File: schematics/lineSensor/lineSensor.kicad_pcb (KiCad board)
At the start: 2 copper layers, 32 parts, among them P1 CONN_01X01, P10 CONN_01X01, P2 CONN_01X01, P3 CONN_01X01, P4 CONN_01X01, P5 CONN_01X01, P6 CONN_01X01, P7 CONN_01X01, P8 CONN_01X01, P9 CONN_01X01

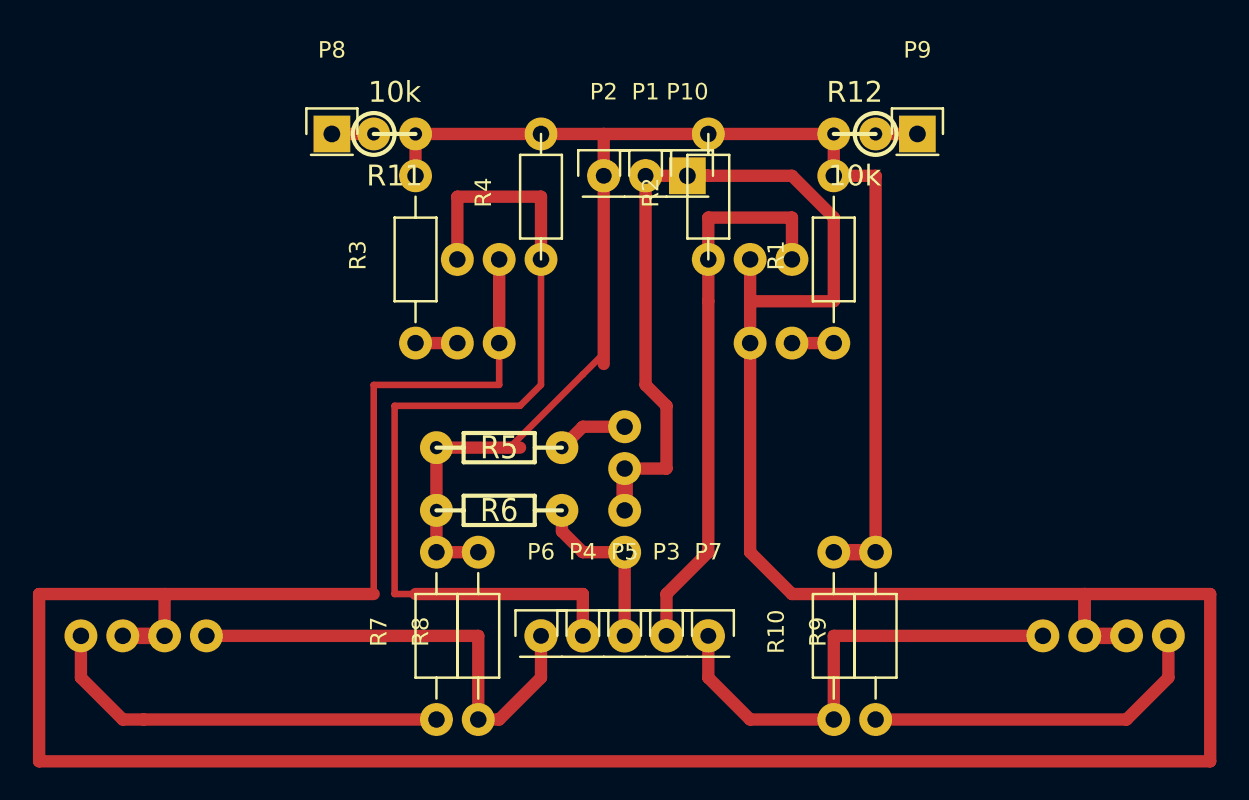
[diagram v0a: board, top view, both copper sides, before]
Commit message: Update lineSensor board for sonar power
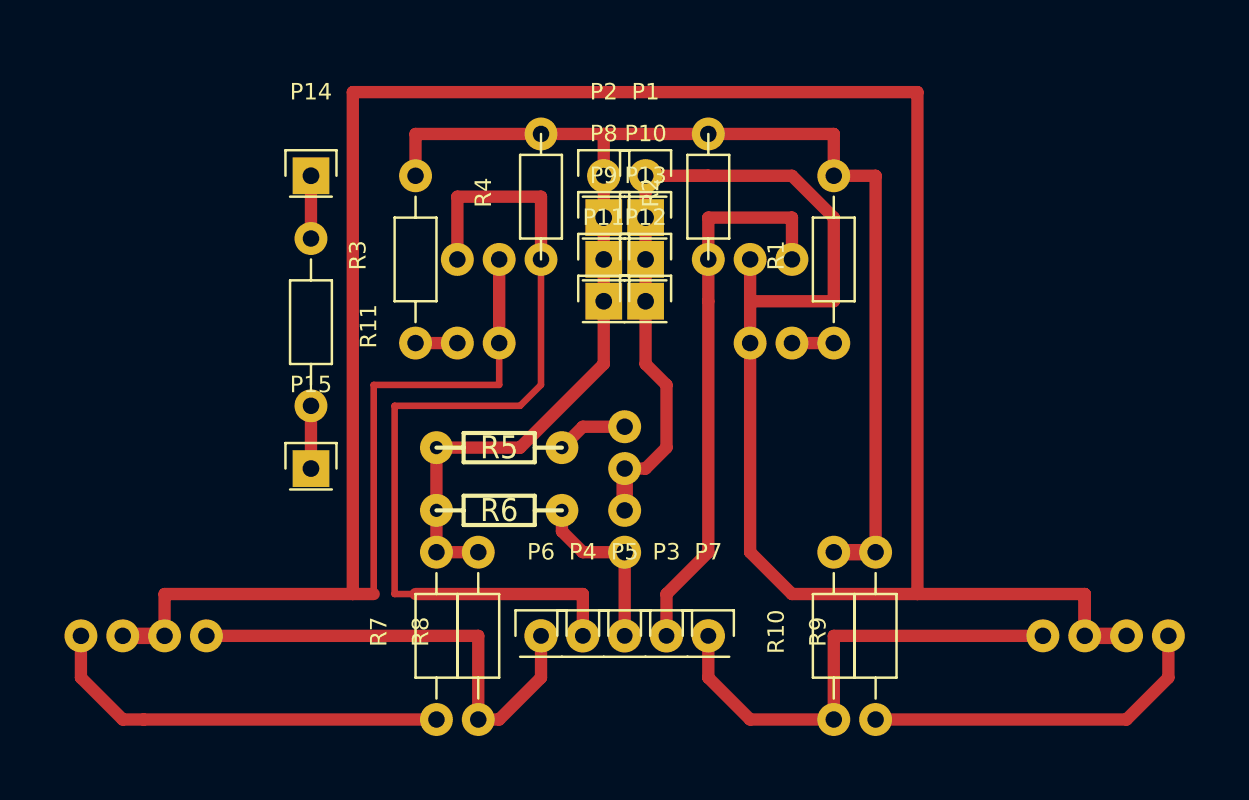
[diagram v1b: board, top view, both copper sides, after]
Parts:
- removed R12: 10k, w_pth_resistors:rc05_vert
- added P11: CONN_01X01, Pin_Headers:Pin_Header_Straight_1x01, F.Cu at (146.1, 109.2)
- added P12: CONN_01X01, Pin_Headers:Pin_Header_Straight_1x01, F.Cu at (148.6, 109.2)
- added P13: CONN_01X01, Pin_Headers:Pin_Header_Straight_1x01, F.Cu at (148.6, 106.7)
- added P14: CONN_01X01, Pin_Headers:Pin_Header_Straight_1x01, F.Cu at (128.3, 101.6)
- added P15: CONN_01X01, Pin_Headers:Pin_Header_Straight_1x01, F.Cu at (128.3, 119.4)
- R11: value 10k -> 8k2; footprint w_pth_resistors:rc05_vert -> Resistors_ThroughHole:Resistor_Horizontal_RM10mm
- moved P9 20.5 mm to (146.1, 106.7)
- moved P8 17.3 mm to (146.1, 104.1)
- moved R11 8.13 mm to (128.3, 105.4), turned to 270 degrees
- moved P10 3.59 mm to (148.6, 104.1)
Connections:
- P2 pad 1: Net-(P2-Pad1) -> Net-(P11-Pad1)
- P8 pad 1: Net-(P8-Pad1) -> Net-(P11-Pad1)
- P9 pad 1: Net-(P9-Pad1) -> Net-(P11-Pad1)
- R1 pad 2: Net-(P2-Pad1) -> Net-(P11-Pad1)
- R10 pad 2: Net-(P2-Pad1) -> Net-(P11-Pad1)
- R11 pad 1: Net-(P8-Pad1) -> Net-(P14-Pad1)
- R11 pad 2: Net-(P2-Pad1) -> Net-(P15-Pad1)
- R2 pad 2: Net-(P2-Pad1) -> Net-(P11-Pad1)
- R3 pad 2: Net-(P2-Pad1) -> Net-(P11-Pad1)
- R4 pad 2: Net-(P2-Pad1) -> Net-(P11-Pad1)
- R5 pad 2: Net-(P2-Pad1) -> Net-(P11-Pad1)
- R6 pad 2: Net-(P2-Pad1) -> Net-(P11-Pad1)
- R7 pad 2: Net-(P2-Pad1) -> Net-(P11-Pad1)
- R8 pad 2: Net-(P2-Pad1) -> Net-(P11-Pad1)
- R9 pad 2: Net-(P2-Pad1) -> Net-(P11-Pad1)
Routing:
- net Net-(P2-Pad1): track 109.7 -> 0.00 mm
- net Net-(P11-Pad1): track 0.00 -> 93.5 mm
- net Net-(D1-Pad2): track 246.5 -> 234.3 mm
- net Net-(P15-Pad1): track 0.00 -> 3.81 mm
- net Net-(P14-Pad1): track 0.00 -> 3.81 mm
- net Net-(P8-Pad1): track 2.54 -> 0.00 mm
- net Net-(P9-Pad1): track 2.54 -> 0.00 mm
